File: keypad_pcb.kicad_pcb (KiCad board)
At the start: 2 copper layers, 103.5 x 99.5 mm, 14 parts

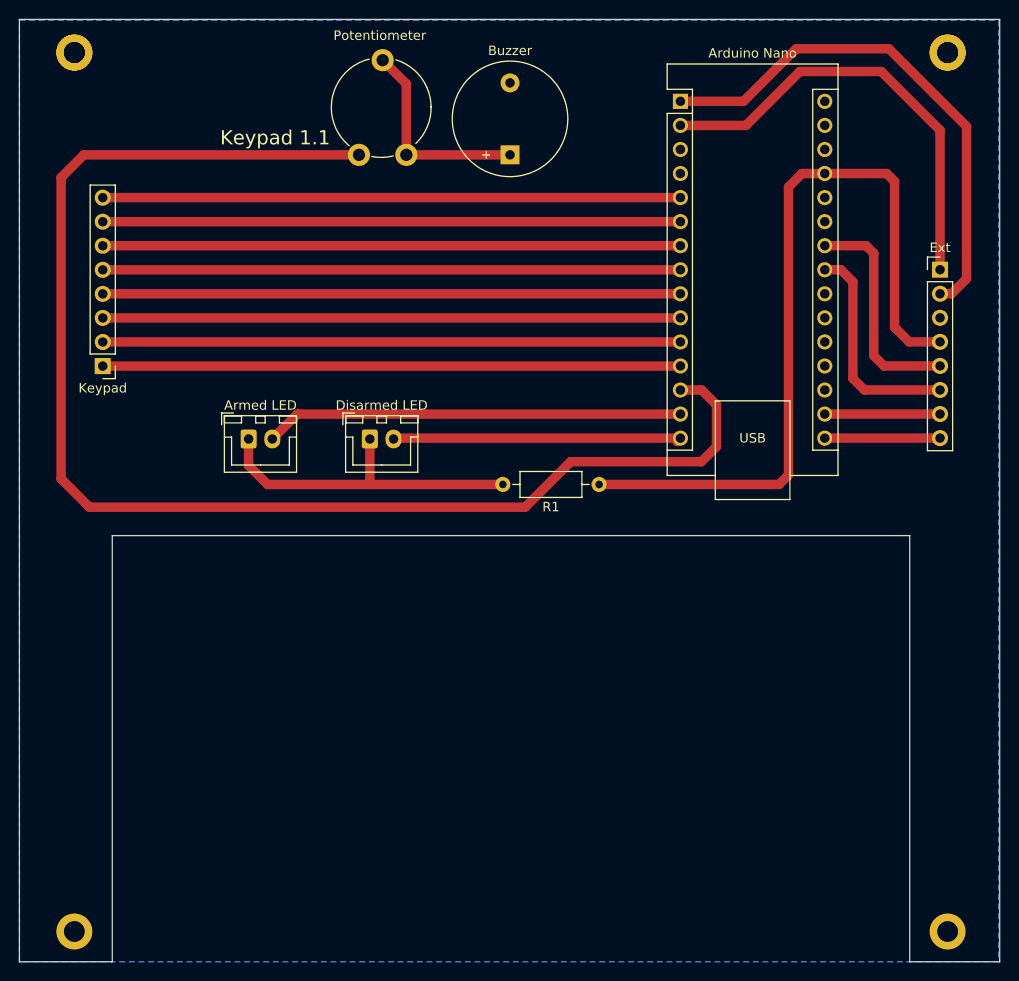
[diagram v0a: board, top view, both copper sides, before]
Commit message: Rework for Arduino Pro Micro
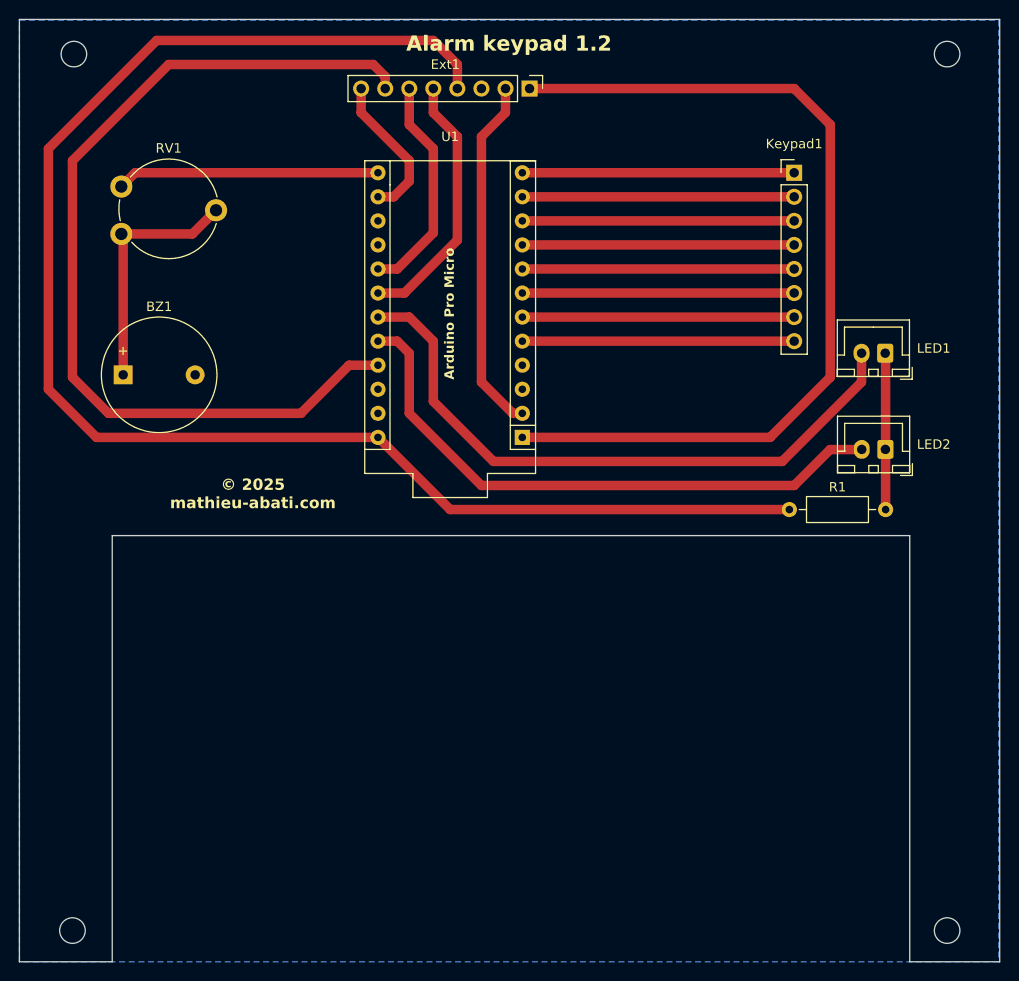
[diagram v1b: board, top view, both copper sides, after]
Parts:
- removed A1: Arduino_Nano_v3.x, Module:Arduino_Nano
- removed REF** (x4): MountingHole_2.2mm_M2_DIN965_Pad, MountingHole:MountingHole_2.2mm_M2_DIN965_Pad
- added ?: , , F.Cu at (194.0, 139.5)
- added ?: , , F.Cu at (101.7, 139.5)
- added G1: LOGO, qr:qr, B.Cu at (162.6, 68.6)
- added U1: Sparkfun_Pro_Micro, Arduino:Sparkfun_Pro_Micro, F.Cu at (133.9, 59.7)
- moved Keypad1 75.8 mm to (177.8, 59.7), turned to 0 degrees
- moved LED1 67.8 mm to (187.4, 78.7), turned to 180 degrees
- moved LED2 54.4 mm to (187.4, 88.9), turned to 180 degrees
- moved Ext1 47.4 mm to (149.9, 50.8), turned to -90 degrees
- moved BZ1 47.0 mm to (107.0, 81.0), turned to 0 degrees
- moved RV1 31.2 mm to (106.8, 66.2), turned to 0 degrees
- moved R1 20.3 mm to (177.3, 95.2), turned to 0 degrees
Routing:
- net Net-(U1-~D10/A10): track 146.2 -> 27.7 mm
- net Net-(Ext1-Pin_7): track 12.2 -> 97.8 mm
- net Net-(Ext1-Pin_4): track 83.8 -> 160.4 mm
- net Net-(Ext1-Pin_1): track 47.1 -> 95.1 mm
- net Net-(Keypad1-Pin_7): track 61.0 -> 28.7 mm
- net Net-(Keypad1-Pin_8): track 61.0 -> 28.7 mm
- net Net-(Keypad1-Pin_6): track 61.0 -> 28.7 mm
- net Net-(Keypad1-Pin_4): track 61.0 -> 28.7 mm
- net Net-(Keypad1-Pin_2): track 61.0 -> 28.7 mm
- net Net-(Keypad1-Pin_5): track 61.0 -> 28.7 mm
- net Net-(Keypad1-Pin_3): track 61.0 -> 28.7 mm
- net Net-(Keypad1-Pin_1): track 61.0 -> 28.7 mm
- net Net-(LED2-Pin_2): track 30.8 -> 62.7 mm
- net Net-(LED1-Pin_2): track 44.2 -> 67.6 mm
- net Net-(LED1-Pin_1): track 35.3 -> 16.6 mm
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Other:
- board text added: "Alarm keypad 1.2"
- board text added: "Arduino Pro Micro"
- board text added: "https://mathieu-abati.com/en/projects/alarm-keypad https://github.com/alarm-keypad/pcb"
- board text added: "© 2025 mathieu-abati.com"
- board text removed: "Keypad 1.1"

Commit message: Update potentiometer to add PCB hole and integrate 3D shape
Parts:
- RV1: footprint Potentiometer_THT:Potentiometer_Piher_PT-10-V10_Vertical -> Potentiometer_THT:Potentiometer_Piher_PT-10-V10_Vertical_Hole
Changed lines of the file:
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@@
 	(net 23 "unconnected-(U1-D14-Pad15)")
 	(net 24 "unconnected-(U1-D15-Pad16)")
-	(footprint "Potentiometer_THT:Potentiometer_Piher_PT-10-V10_Vertical"
+	(footprint "Potentiometer_THT:Potentiometer_Piher_PT-10-V10_Vertical_Hole"
 		(layer "F.Cu")
 		(at 106.76 66.15)
-		(descr "Potentiometer, vertical, Piher PT-10-V10, http://www.piher-nacesa.com/pdf/12-PT10v03.pdf")
-		(tags "Potentiometer vertical Piher PT-10-V10")
+		(descr "Potentiometer, vertical, shaft hole, Piher PT-10-V10, http://www.piher-nacesa.com/pdf/12-PT10v03.pdf")
+		(tags "Potentiometer vertical hole Piher PT-10-V10")
 		(property "Reference" "RV1"
 			(at 5 -9.05 0)
@@
 		(fp_circle
 			(center 5 -2.65)
-			(end 6.5 -2.65)
-			(stroke
-				(width 0.1)
-				(type solid)
-			)
-			(fill no)
-			(layer "F.Fab")
-		)
-		(fp_circle
-			(center 5 -2.65)
 			(end 10.15 -2.65)
 			(stroke
@@
 				)
 			)
+		)
+		(pad "" np_thru_hole circle
+			(at 5 -2.65)
+			(size 4 4)
+			(drill 4)
+			(layers "*.Cu" "*.Mask")
 		)
 		(pad "1" thru_hole circle
@@
 		)
 		(embedded_fonts no)
-		(model "${KICAD9_3DMODEL_DIR}/Potentiometer_THT.3dshapes/Potentiometer_Piher_PT-10-V10_Vertical.step"
+		(model "${KICAD9_3DMODEL_DIR}/Potentiometer_THT.3dshapes/Potentiometer_Piher_PT-10-V10_Vertical_Hole.step"
 			(offset
 				(xyz 0 0 0)

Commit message: Fixes to be ready to generate gerber
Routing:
- net Net-(BZ1--): track 26.0 -> 26.8 mm
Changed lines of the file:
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@@
 		(model "${KICAD9_3DMODEL_DIR}/Potentiometer_THT.3dshapes/Potentiometer_Piher_PT-10-V10_Vertical_Hole.step"
 			(offset
-				(xyz 0 0 0)
+				(xyz 0 0 1)
 			)
 			(scale
@@
 			)
 			(rotate
-				(xyz 0 0 0)
+				(xyz -0 -0 -0)
+			)
+		)
+		(model "${PIHER}/PT-10.stp"
+			(offset
+				(xyz 5 2.5 1.5)
+			)
+			(scale
+				(xyz 0.1 0.1 0.1)
+			)
+			(rotate
+				(xyz -90 -0 90)
 			)
 		)
@@
 	)
 	(gr_text "https://mathieu-abati.com/en/projects/alarm-keypad\nhttps://github.com/alarm-keypad/pcb"
-		(at 170.18 96.52 0)
+		(at 170.18 93.98 0)
 		(layer "B.SilkS")
 		(effects
@@
 	)
 	(segment
-		(start 114.26 66.15)
-		(end 116.76 63.65)
+		(start 106.954 68.58)
+		(end 106.954 66.344)
+		(width 1)
+		(layer "F.Cu")
+		(net 2)
+	)
+	(segment
+		(start 106.954 81.026)
+		(end 106.954 68.58)
 		(width 1)
 		(layer "F.Cu")
@@
 	)
 	(segment
-		(start 106.76 66.15)
-		(end 114.26 66.15)
+		(start 106.954 66.344)
+		(end 106.76 66.15)
 		(width 1)
 		(layer "F.Cu")
@@
 	)
 	(segment
-		(start 106.954 81.026)
-		(end 106.954 66.344)
+		(start 111.83 68.58)
+		(end 106.954 68.58)
 		(width 1)
 		(layer "F.Cu")
@@
 	)
 	(segment
-		(start 106.954 66.344)
-		(end 106.76 66.15)
+		(start 116.76 63.65)
+		(end 111.83 68.58)
 		(width 1)
 		(layer "F.Cu")
